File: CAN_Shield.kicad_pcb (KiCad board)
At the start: 2 copper layers, 65 x 56 mm, 20 parts, among them J1 GPIO, U1 MX128-5.08-09P-GN01-CU-Y-A, U2 MCP2515T-I/SO, U4 SN65HVD230DR, X1 X322516MLB4SI

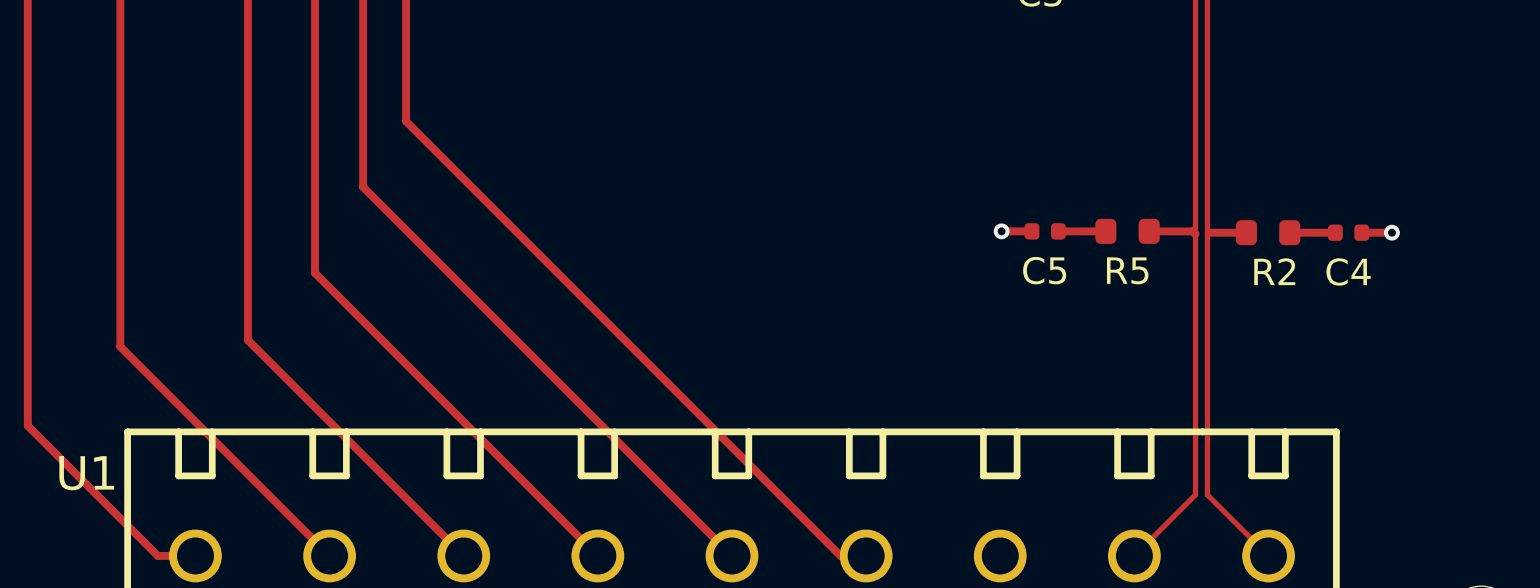
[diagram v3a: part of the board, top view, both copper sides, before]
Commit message: add silk screen for pin of screw terminal
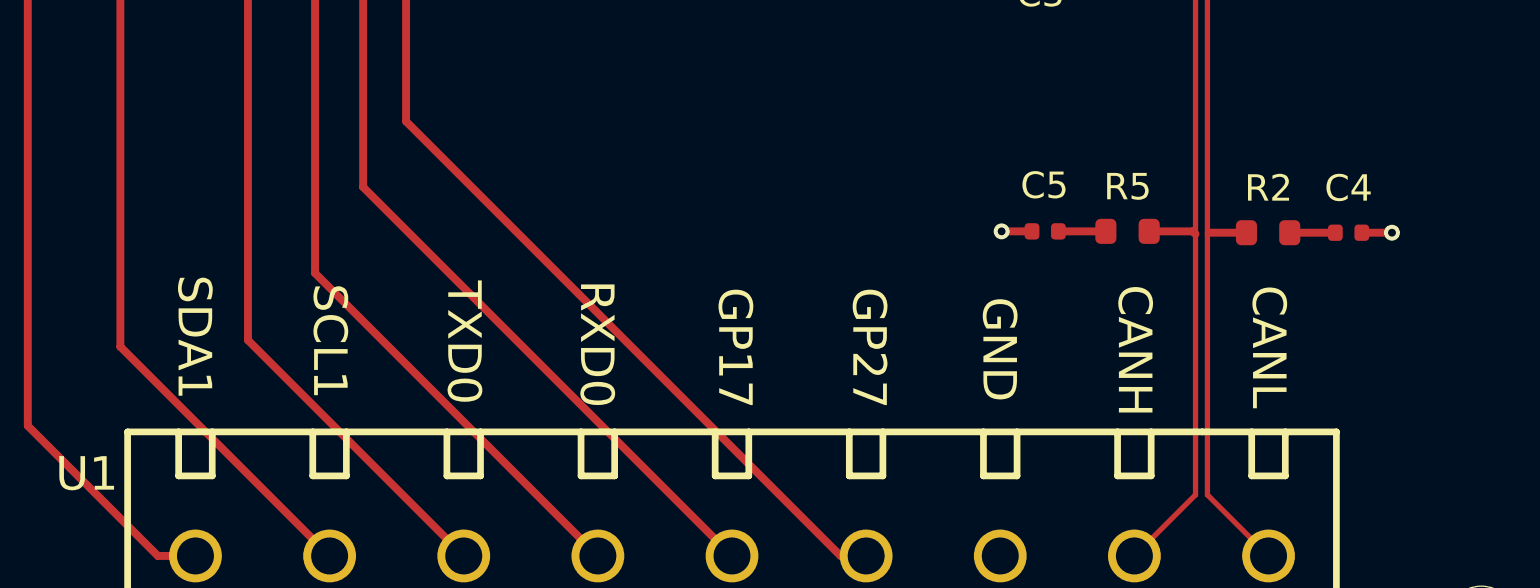
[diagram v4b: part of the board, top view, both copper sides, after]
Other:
- board text added: "CANH"
- board text added: "CANL"
- board text added: "GND"
- board text added: "GP17"
- board text added: "GP27"
- board text added: "RXD0"
- board text added: "SCL1"
- board text added: "SDA1"
- board text added: "TXD0"
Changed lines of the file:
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@@
 		(tags "capacitor")
 		(property "Reference" "C5"
-			(at 0 -1.524 0)
+			(at 0.0254 1.7272 0)
 			(layer "F.SilkS")
 			(effects
@@
 		(tags "resistor")
 		(property "Reference" "R5"
-			(at 0 -1.524 0)
+			(at -0.0072 1.6764 0)
 			(layer "F.SilkS")
 			(effects
@@
 		(tags "capacitor")
 		(property "Reference" "C4"
-			(at 0 1.524 0)
+			(at 0 -1.6764 0)
 			(layer "F.SilkS")
 			(effects
@@
 		(tags "resistor")
 		(property "Reference" "R2"
-			(at 0.254 1.524 0)
+			(at 0.0174 -1.6764 0)
 			(layer "F.SilkS")
 			(effects
@@
 		(layer "Edge.Cuts")
 	)
+	(gr_text "RXD0"
+		(at 127.9908 85.9792 270)
+		(layer "F.SilkS")
+		(effects
+			(font
+				(size 1.27 1.27)
+				(thickness 0.15)
+			)
+		)
+	)
+	(gr_text "SDA1"
+		(at 112.7508 85.7252 270)
+		(layer "F.SilkS")
+		(effects
+			(font
+				(size 1.27 1.27)
+				(thickness 0.15)
+			)
+		)
+	)
+	(gr_text "GP17"
+		(at 133.2232 86.1316 270)
+		(layer "F.SilkS")
+		(effects
+			(font
+				(size 1.27 1.27)
+				(thickness 0.15)
+			)
+		)
+	)
+	(gr_text "GP27"
+		(at 138.3032 86.1316 270)
+		(layer "F.SilkS")
+		(effects
+			(font
+				(size 1.27 1.27)
+				(thickness 0.15)
+			)
+		)
+	)
+	(gr_text "TXD0"
+		(at 122.9616 85.9284 270)
+		(layer "F.SilkS")
+		(effects
+			(font
+				(size 1.27 1.27)
+				(thickness 0.15)
+			)
+		)
+	)
+	(gr_text "CANL"
+		(at 153.4416 86.0808 270)
+		(layer "F.SilkS")
+		(effects
+			(font
+				(size 1.27 1.27)
+				(thickness 0.15)
+			)
+		)
+	)
+	(gr_text "CANH"
+		(at 148.3616 86.2332 270)
+		(layer "F.SilkS")
+		(effects
+			(font
+				(size 1.27 1.27)
+				(thickness 0.15)
+			)
+		)
+	)
+	(gr_text "GND"
+		(at 143.2308 86.1824 270)
+		(layer "F.SilkS")
+		(effects
+			(font
+				(size 1.27 1.27)
+				(thickness 0.15)
+			)
+		)
+	)
+	(gr_text "SCL1"
+		(at 117.8816 85.8776 270)
+		(layer "F.SilkS")
+		(effects
+			(font
+				(size 1.27 1.27)
+				(thickness 0.15)
+			)
+		)
+	)
 	(gr_text "USB"

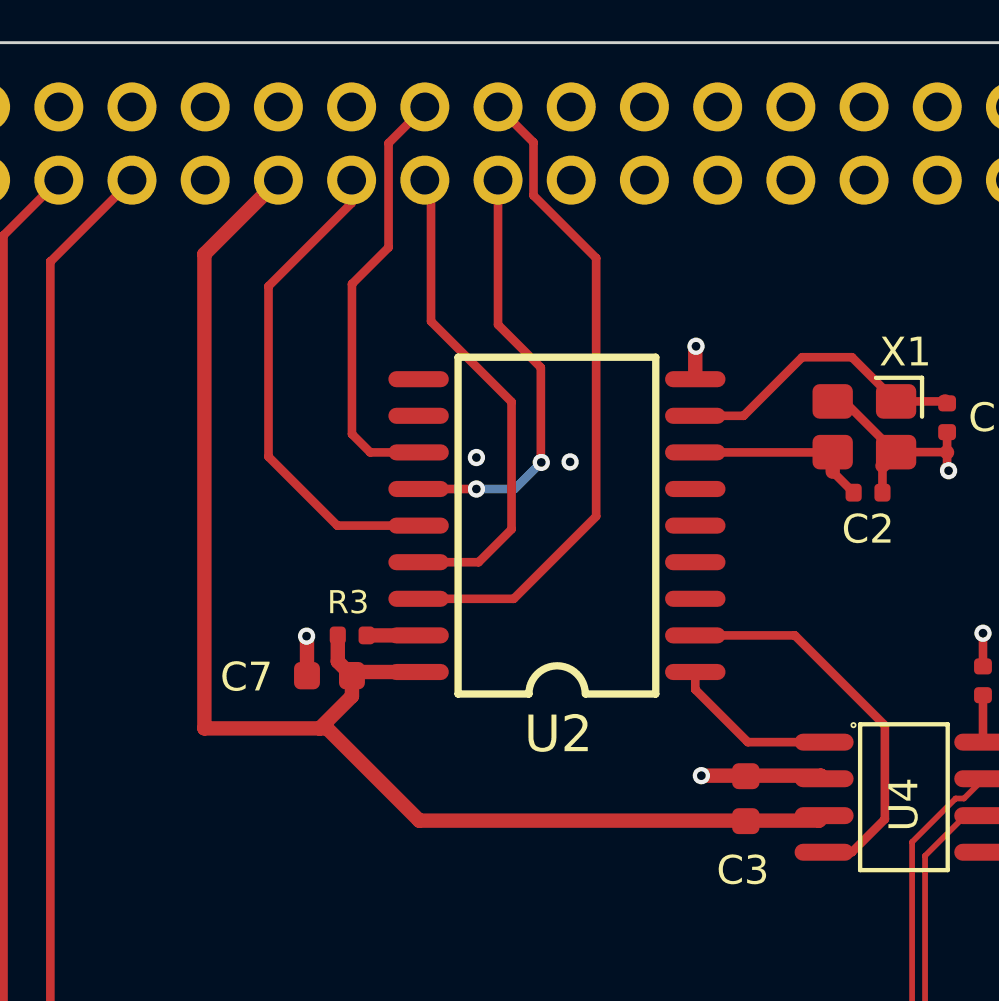
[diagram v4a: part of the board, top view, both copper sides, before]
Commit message: fix erc (thermal relief connection to zone incomplete (min spoke count 2 actual 1) by edit thermal relief gap from 0.5 to 0.3 mm
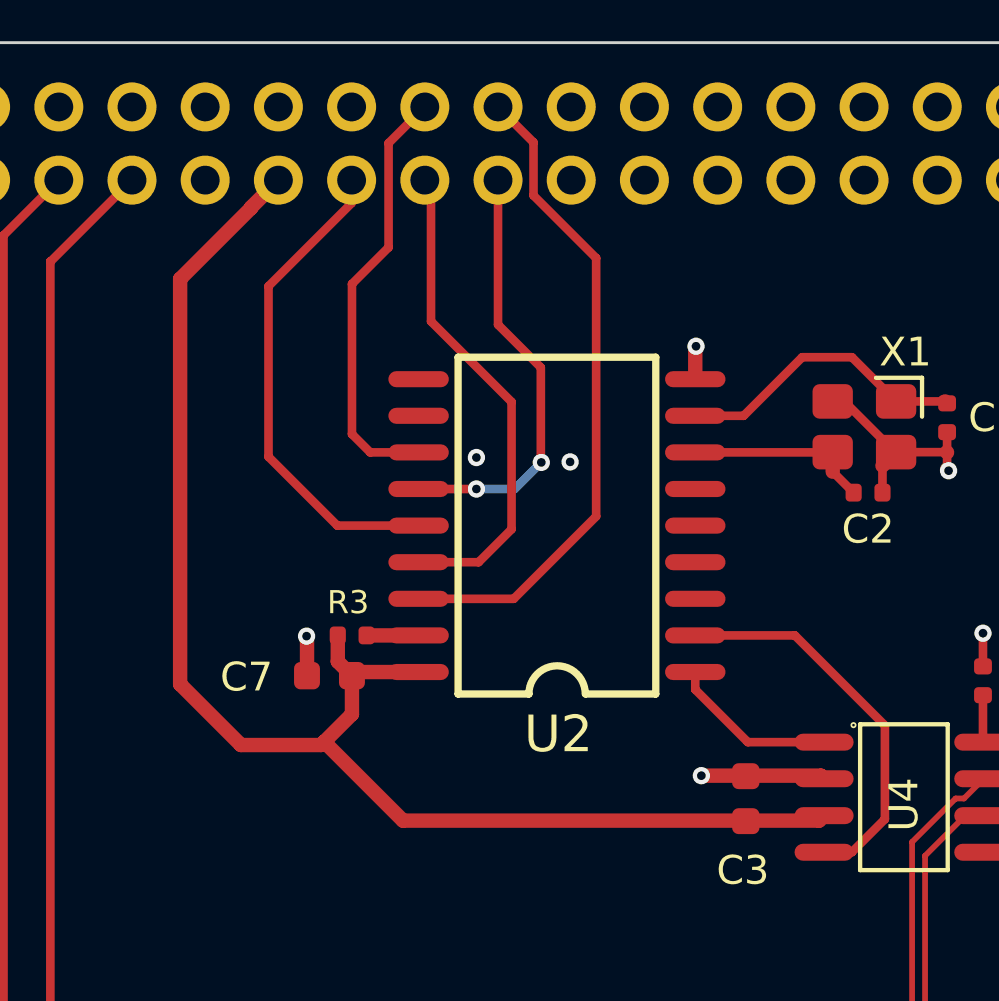
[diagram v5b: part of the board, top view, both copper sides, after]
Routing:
- net +3V3: track 49.2 -> 50.0 mm

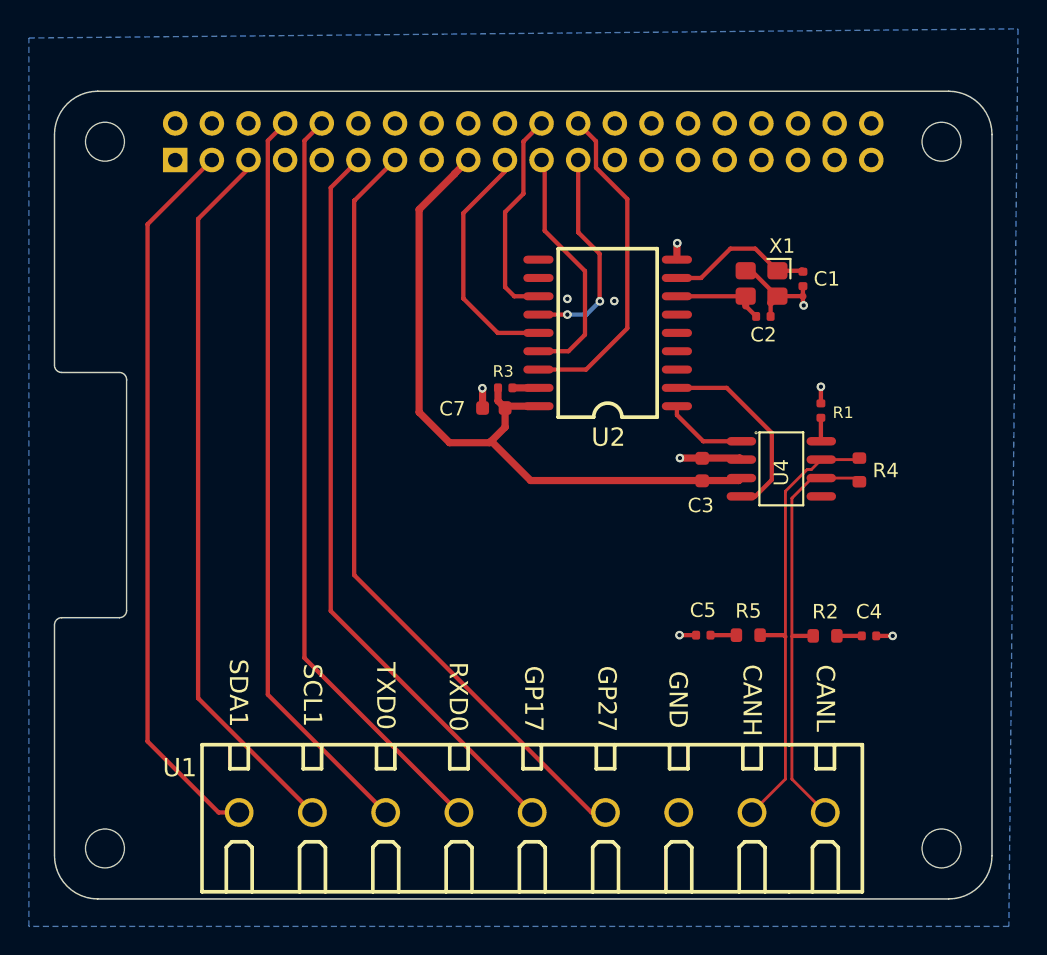
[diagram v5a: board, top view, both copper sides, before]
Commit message: change can diff pair trace width to 0.35 mm get 133ohm zdiff
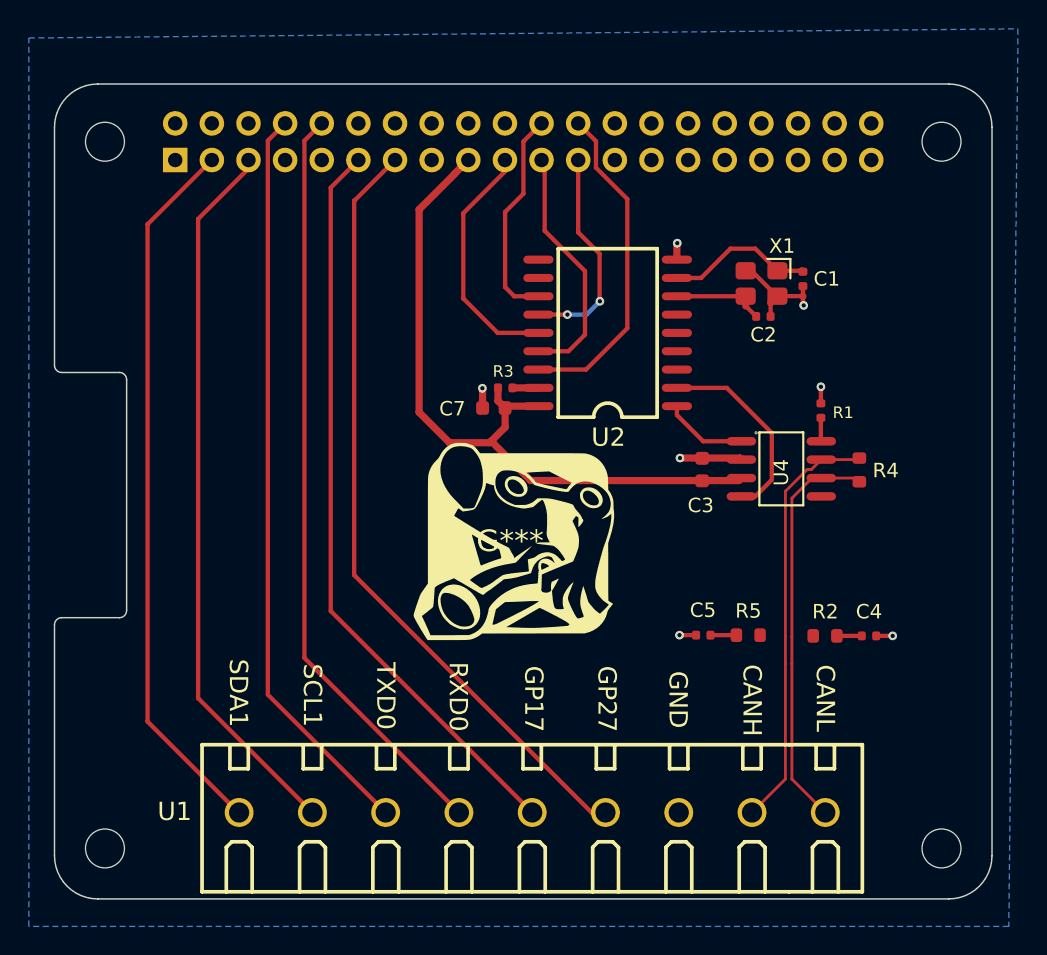
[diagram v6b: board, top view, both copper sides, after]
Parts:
- added G***: LOGO, LOGO, F.Cu at (131.6, 75.2)
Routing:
- net /CAN_D+: track 31.1 -> 29.3 mm
- net /CAN_D-: track 29.5 -> 28.1 mm
- net /GPIO2/SDA1: track 50.5 -> 49.7 mm
- net GND: vias 9 -> 7
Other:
- board size 65 x 56 mm -> 65 x 56.5 mm

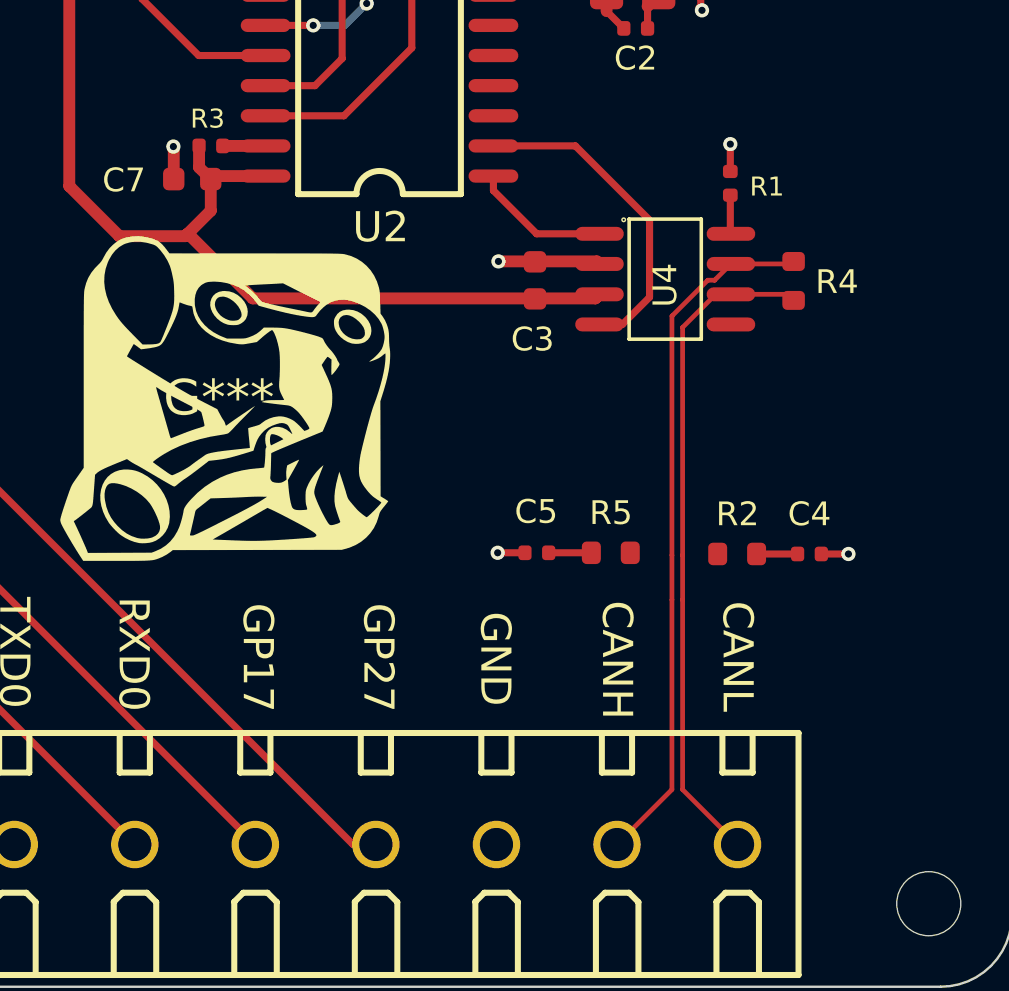
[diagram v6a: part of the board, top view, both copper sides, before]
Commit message: tune CAN diff pair skew
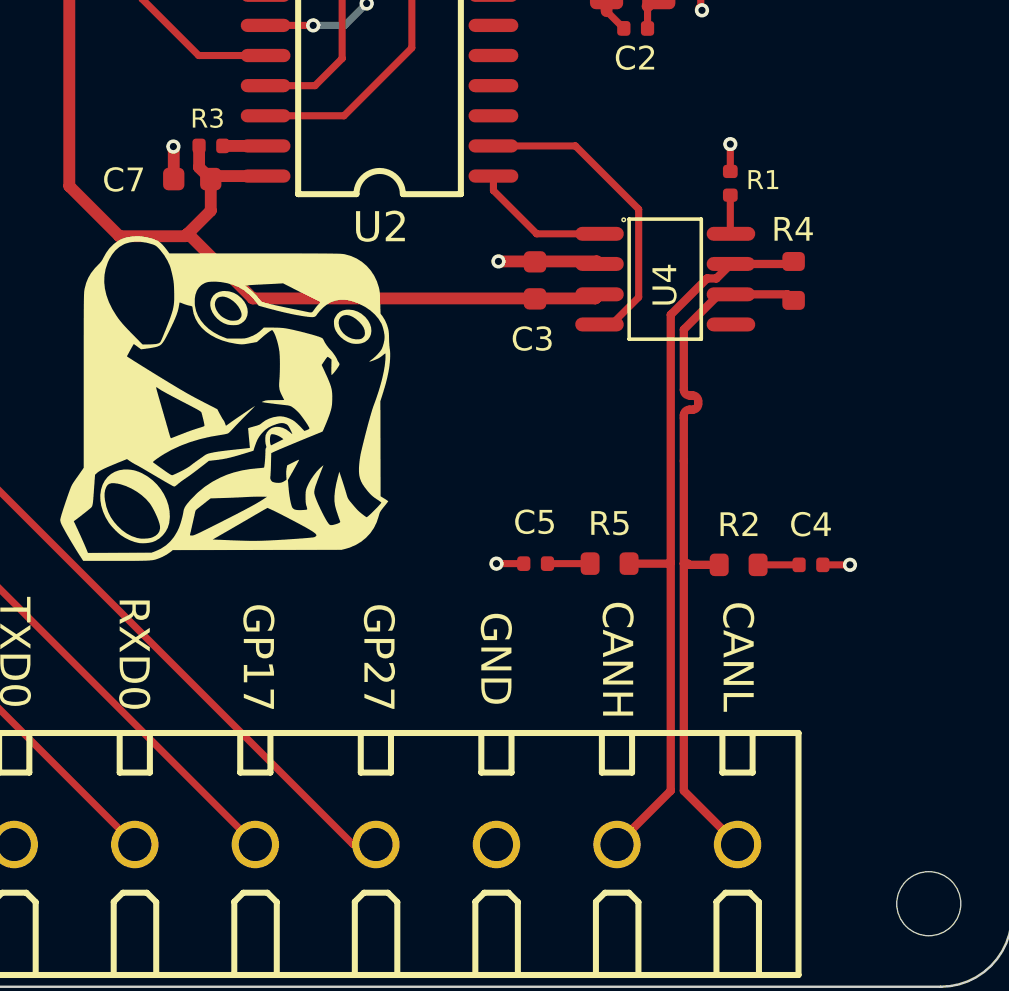
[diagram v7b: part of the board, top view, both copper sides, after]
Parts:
- moved C4 0.46 mm to (156.5, 82.2)
- moved R2 0.46 mm to (153.5, 82.2)
- moved R5 0.46 mm to (148.0, 82.2)
- moved C5 0.46 mm to (144.9, 82.2)
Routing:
- net /CAN_D-: track 28.1 -> 30.3 mm
- net /CAN_D+: track 29.3 -> 31.2 mm
- net /RXCAN: track 13.7 -> 13.1 mm
